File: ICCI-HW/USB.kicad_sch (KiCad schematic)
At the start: 29 parts

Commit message: schematic V1.0
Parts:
- removed C?: x, Capacitor_SMD:C_0603_1608Metric, symbol Device:C
- C201: renamed from C?; value x -> 100n
- FB201: renamed from FB?; value FerriteBead -> 120ohm @ 100MHz
- R209, R210: renamed from R?; value 680R -> 510R
- gave numbers to parts that had none: 24
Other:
- note added: "Test for best EMI solution Probably need to be grounded for OTG (?)."
- note removed: "Test for best EMI solution"
- moved on the sheet: FB201

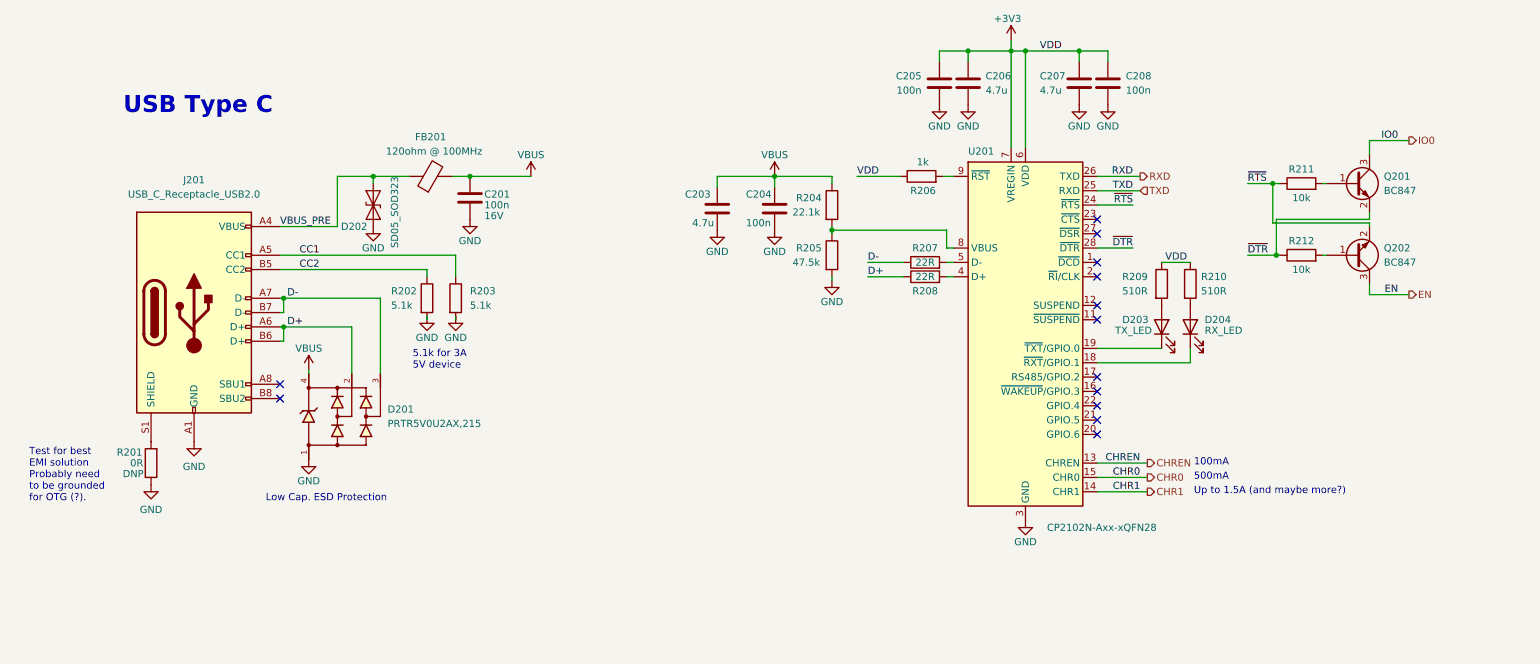
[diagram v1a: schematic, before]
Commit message: footprint assigned
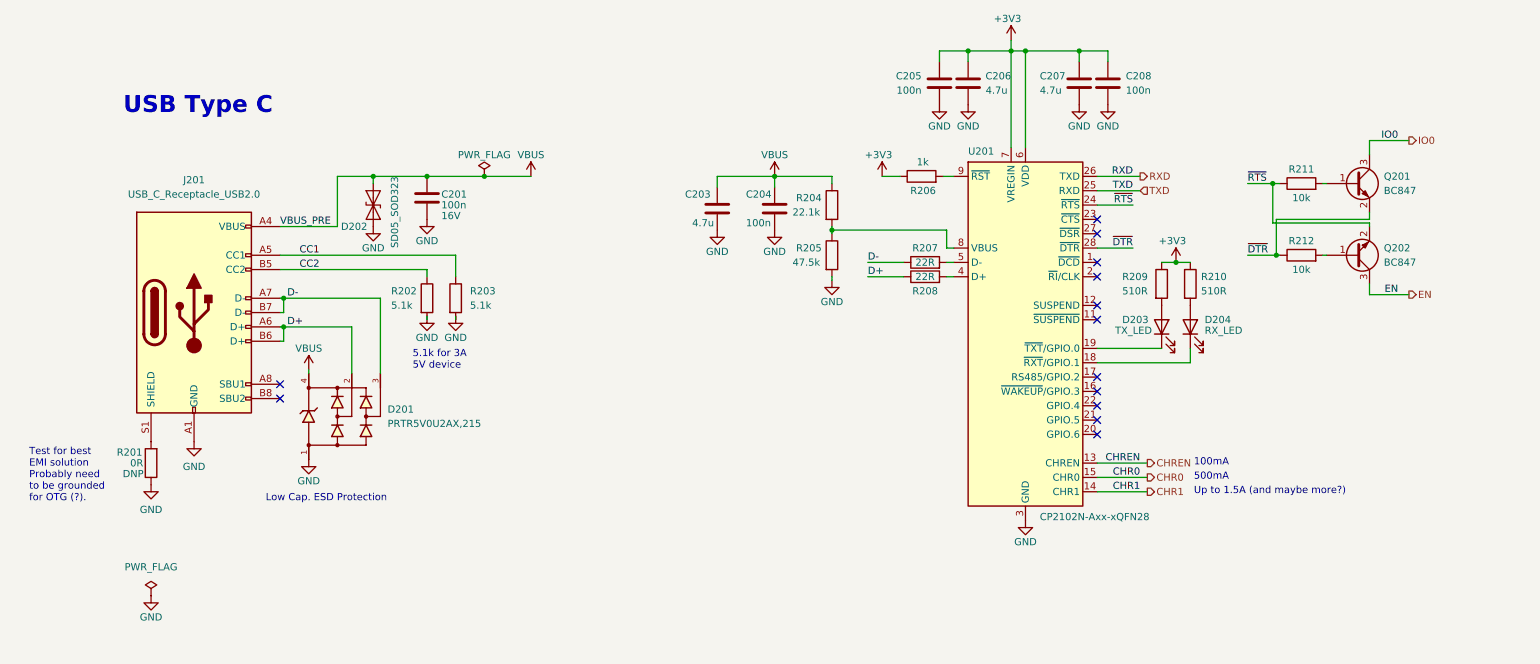
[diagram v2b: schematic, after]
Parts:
- removed FB201: 120ohm @ 100MHz, Inductor_SMD:L_0603_1608Metric, symbol Device:FerriteBead
- C201: footprint Capacitor_SMD:C_0805_2012Metric -> Capacitor_SMD:C_0603_1608Metric
- C203, C204, C205, C206, C207, C208: footprint (none) -> Capacitor_SMD:C_0603_1608Metric
- D201: footprint (none) -> Package_TO_SOT_SMD:SOT-143
- D203, D204: footprint (none) -> LED_SMD:LED_0805_2012Metric
- J201: footprint Connector_USB:USB_C_Receptacle_Amphenol_12401548E4-2A -> ICCI-LIB:USB_C_Receptacle_Amphenol_12401548E4-2A
- R201, R202, R203, R204, R205, R206, R207, R208, R209, R210, R211, R212: footprint (none) -> Resistor_SMD:R_0603_1608Metric
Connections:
- net VBUS_PRE is gone; now on net VBUS: D202.2 (A2), J201.A4 (VBUS), J201.A9 (VBUS), J201.B4 (VBUS), J201.B9 (VBUS)
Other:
- moved on the sheet: C201

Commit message: fw: updates
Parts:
- removed Q201, Q202: BC847, Package_TO_SOT_SMD:SOT-23, symbol Transistor_BJT:BC847
- removed R211, R212: 10k, Resistor_SMD:R_0603_1608Metric, symbol Device:R
- added Q201, Q202: PDTC114Y, Package_TO_SOT_SMD:SOT-23, symbol Transistor_BJT:DTC114Y
- C201: Voltage 16V -> (none)
- renumbered C203 to C202, C204 to C203, C205 to C204, C206 to C205, C207 to C206, C208 to C207
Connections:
- net EN: now also Q202.3 (C)
- net IO0: now also Q201.3 (C)
- net ~{DTR}: now also Q201.2 (E), Q202.1 (B)
- net ~{RTS}: now also Q201.1 (B), Q202.2 (E)

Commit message: hw: updates
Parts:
- added NT201: NetTie_2, NetTie:NetTie-2_SMD_Pad0.5mm, symbol Device:NetTie_2
- added Q203: NX7002AK, Package_TO_SOT_SMD:SOT-23, symbol Device:Q_NMOS_GSD
- R201: now in the parts list
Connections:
- net D+: now also NT201.1, Q203.3 (D)
- net D-: now also NT201.2
- net GND: now also Q203.2 (S)
- net at U201.17 (RS485/GPIO.2): now also Q203.1 (G)
- no-connect marks 13 -> 12
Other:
- note added: "Bootloader Mode from USB"
- note added: "CP2102N GPIO must be configured for Battery Charging using Xpress Configurator (see Datasheet)."
- note added: "Test for best EMI solution. Probably need to be grounded considering OTG (?)."
- note added: "USB to UART"
- note added: "Up to 1.5A"
- note added: "Workaround for known silicon issue (CP2102N_E110), GPIO2 need to be set with Xpress Configurator, see Errata."
- note removed: "Test for best EMI solution Probably need to be grounded for OTG (?)."
- note removed: "Up to 1.5A (and maybe more?)"
- company: tollsimy -> Simone Tollardo
- moved on the sheet: C201, C202, C203, C204, C205, C206, C207, D201, D202, D203, D204, J201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

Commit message: hw: updates
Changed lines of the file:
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@@
   (symbol (lib_id "Device:C") (at 201.93 62.865 0) (unit 1)
     (in_bom yes) (on_board yes)
-    (property "Reference" "C206" (id 0) (at 194.945 61.595 0)
+    (property "Reference" "C206" (id 0) (at 194.31 61.595 0)
       (effects (font (size 1.27 1.27)) (justify left))
     )

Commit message: start layout
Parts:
- removed NT201: NetTie_2, NetTie:NetTie-2_SMD_Pad0.5mm, symbol Device:NetTie_2
- added Q204: NX7002AK, Package_TO_SOT_SMD:SOT-23, symbol Device:Q_NMOS_GSD
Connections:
- net D-: now also Q204.3 (D)
- net GND: now also Q204.2 (S)
- net at Q203.1 (G), U201.17 (RS485/GPIO.2): now also Q204.1 (G)
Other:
- moved on the sheet: Q201, Q202, Q203
